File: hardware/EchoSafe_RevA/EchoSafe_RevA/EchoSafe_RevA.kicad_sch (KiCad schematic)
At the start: 37 parts, among them J1 TP4056_Module, M1 C0720B001F, M2 C0720B001F, M3 C0720B001F, M4 C0720B001F, U1 ESP32-S3-WROOM-1-N16R8, U2 MAX98357AETE+T, U3 DRV2605LDGS, U5 TCA9548A, U6 DRV2605LDGS, U7 DRV2605LDGS, U8 DRV2605LDGS

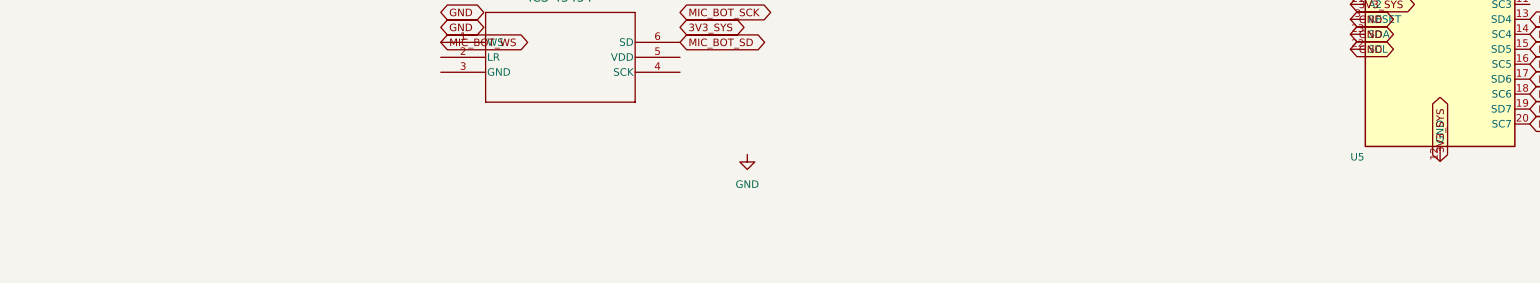
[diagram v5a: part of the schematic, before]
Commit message: Add per-module wire harness connectors (star topology)
Adds J2 (Front-Left, 9 pins), J3 (Front-Right, 9 pins), J4 (Rear-Left,
7 pins), J5 (Rear-Right, 7 pins) -- placeholder generic connectors
documenting the exact conductor count and signal list each earpiece
module's cable needs, per the confirmed board partition:

- Front modules (J2/J3): WS, BCLK, DOUT, 3V3_SYS, GND, motor OUTP/OUTN,
  speaker OUTP/OUTN
- Rear modules (J4/J5): same minus the speaker pair

Star topology confirmed with the user: each module gets its own full
copy of the shared mic I2S bus via a separate cable, rather than one
cable daisy-chaining through both mics on a pair. The electrical nets
are unchanged either way (both mics on a pair always share the same
ESP32 pins) -- the topology choice only affects physical cable routing
and how many pins the central pod's connectors need.

Documented that each mic's SEL pin does not need a dedicated harness
wire (it's a static tie, wired locally using the 3V3_SYS/GND already
present at the module for mic power), and that each mic's decoupling
cap (C9-C12) travels with its mic to the earpiece module rather than
staying centralized -- decoupling only works close to the pin it
protects.

Verified: whole-file paren balance intact, 475 unique UUIDs, no
duplicate references, correct net endpoint counts on every affected
signal, no coordinate conflicts.

Co-Authored-By: Claude Sonnet 5 <noreply@anthropic.com>
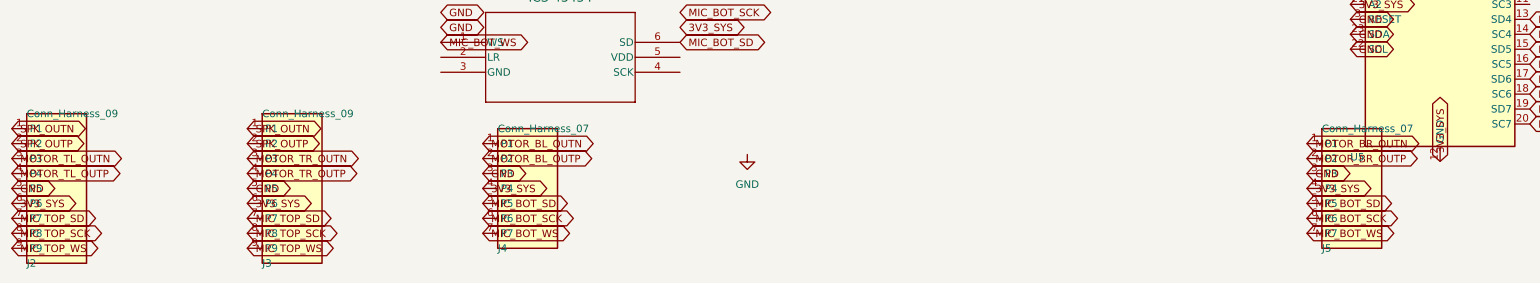
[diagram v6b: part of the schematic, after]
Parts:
- added J2, J3: Conn_Harness_09, symbol Connector:Conn_Harness_09
- added J4, J5: Conn_Harness_07, symbol Connector:Conn_Harness_07
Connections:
- net 3V3_SYS: now also J2.6 (P6), J3.6 (P6), J4.4 (P4), J5.4 (P4)
- net GND: now also J2.5 (P5), J3.5 (P5), J4.3 (P3), J5.3 (P3)
- net MIC_BOT_SCK: now also J4.6 (P6), J5.6 (P6)
- net MIC_BOT_SD: now also J4.5 (P5), J5.5 (P5)
- net MIC_BOT_WS: now also J4.7 (P7), J5.7 (P7)
- net MIC_TOP_SCK: now also J2.8 (P8), J3.8 (P8)
- net MIC_TOP_SD: now also J2.7 (P7), J3.7 (P7)
- net MIC_TOP_WS: now also J2.9 (P9), J3.9 (P9)
- net MOTOR_BL_OUTN: now also J4.1 (P1)
- net MOTOR_BL_OUTP: now also J4.2 (P2)
- net MOTOR_BR_OUTN: now also J5.1 (P1)
- net MOTOR_BR_OUTP: now also J5.2 (P2)
- net MOTOR_TL_OUTN: now also J2.3 (P3)
- net MOTOR_TL_OUTP: now also J2.4 (P4)
- net MOTOR_TR_OUTN: now also J3.3 (P3)
- net MOTOR_TR_OUTP: now also J3.4 (P4)
- net SPK_OUTN: now also J2.1 (P1), J3.1 (P1)
- net SPK_OUTP: now also J2.2 (P2), J3.2 (P2)

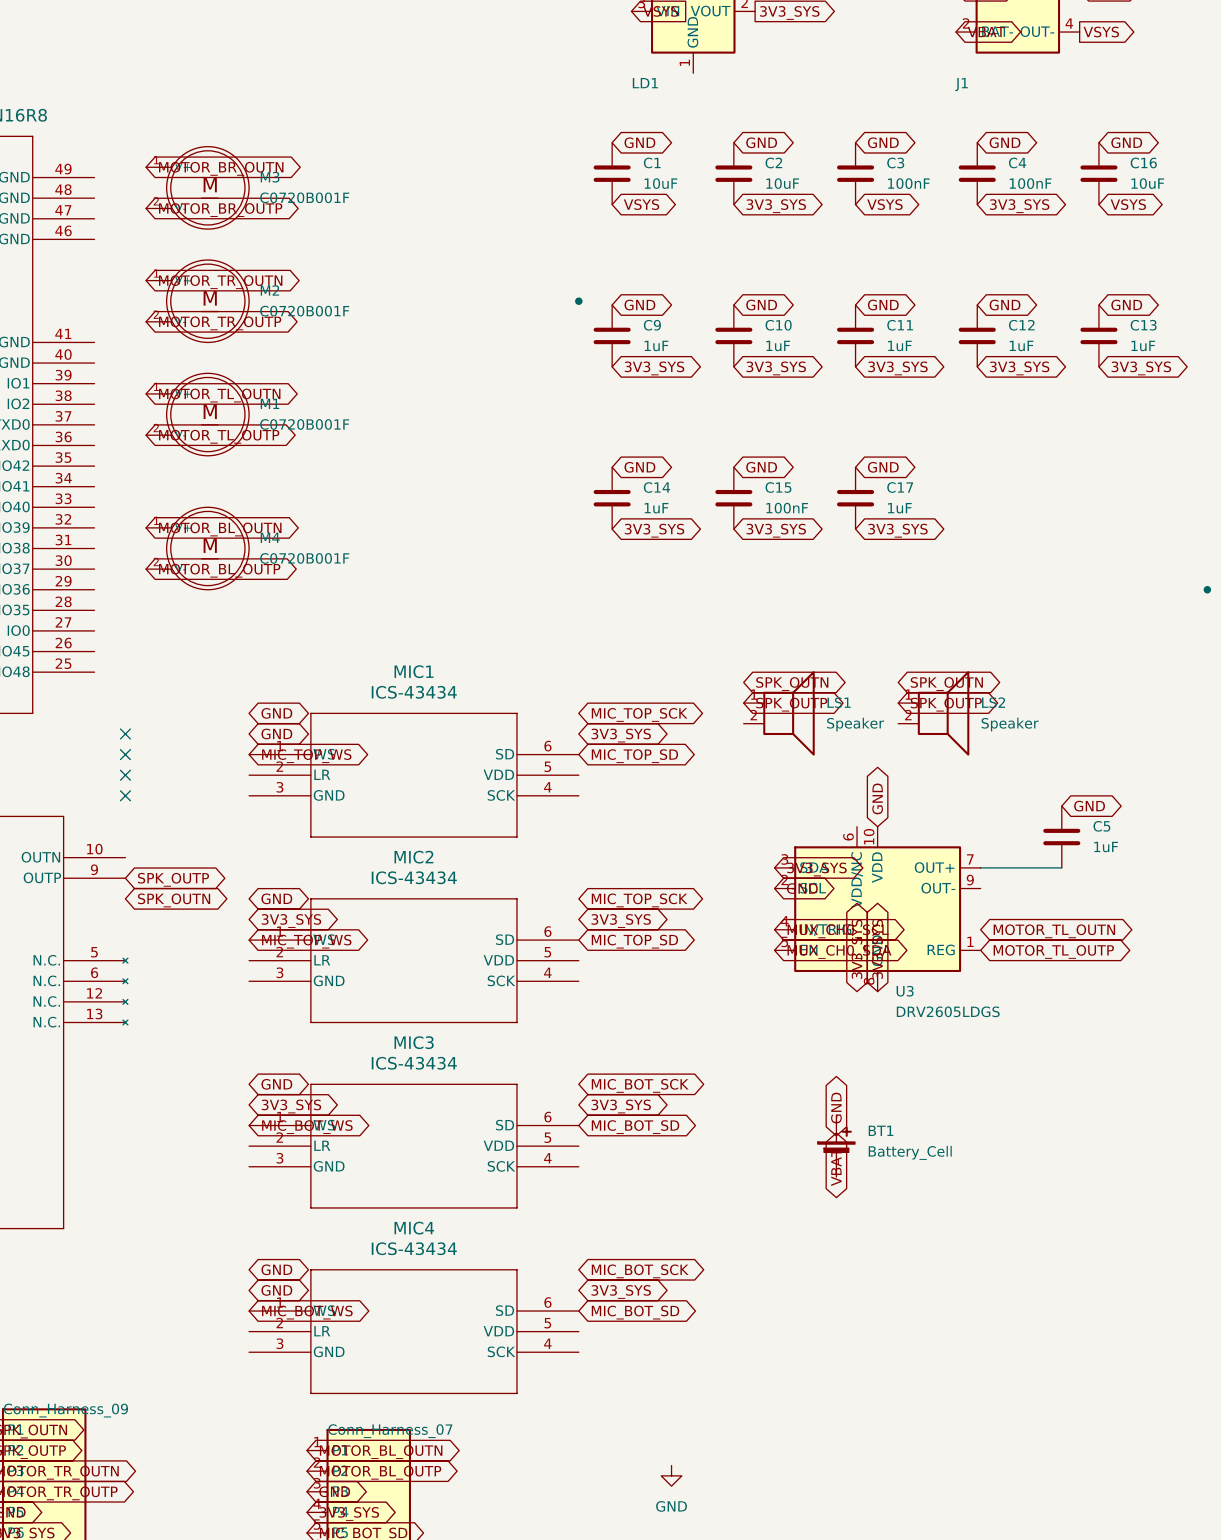
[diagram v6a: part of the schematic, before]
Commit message: Split hardware into 5 separate KiCad projects (central pod + 4 modules)
EchoSafe_RevA now specifically represents the central pod. Created 4 new
small KiCad projects for the earpiece modules, each with its own
.kicad_pro/.kicad_sch/sym-lib-table:

- EchoSafe_FrontLeft:  MIC1, M1, LS1, C9  (9-pin connector, has speaker)
- EchoSafe_FrontRight: MIC2, M2, LS2, C10 (9-pin connector, has speaker)
- EchoSafe_RearLeft:   MIC4, M4, C12      (7-pin connector, no speaker)
- EchoSafe_RearRight:  MIC3, M3, C11      (7-pin connector, no speaker)

All 4 new projects share the existing library folder
(EchoSafe_RevA/lib/symbols/) via relative sym-lib-table paths -- nothing
duplicated. Each module has its own local J1 connector wired with the
same net names as the corresponding pod-side connector (J2/J3/J4/J5);
matching names is a documentation convention across independent
projects, not an automatic KiCad link -- the physical cable is the real
connection.

Removed MIC1-4, M1-4, LS1-2, and C9-C12 (their decoupling caps) from the
central pod's schematic entirely -- both the component instances and
their pin-level net labels -- verifying net-by-net that only the
endpoints which moved out were removed (e.g. MIC_TOP_WS dropped from 5
endpoints to 3: ESP32 + the two pod-side connectors, matching what
should remain).

Verified independently: all 5 .kicad_sch files have balanced parens and
unique UUIDs within their own file (no cross-project uniqueness
requirement -- separate projects, separate namespaces); the central
pod's shared nets (3V3_SYS, GND, motor/speaker/mic buses) retain exactly
the endpoints that should still be there.

Co-Authored-By: Claude Sonnet 5 <noreply@anthropic.com>
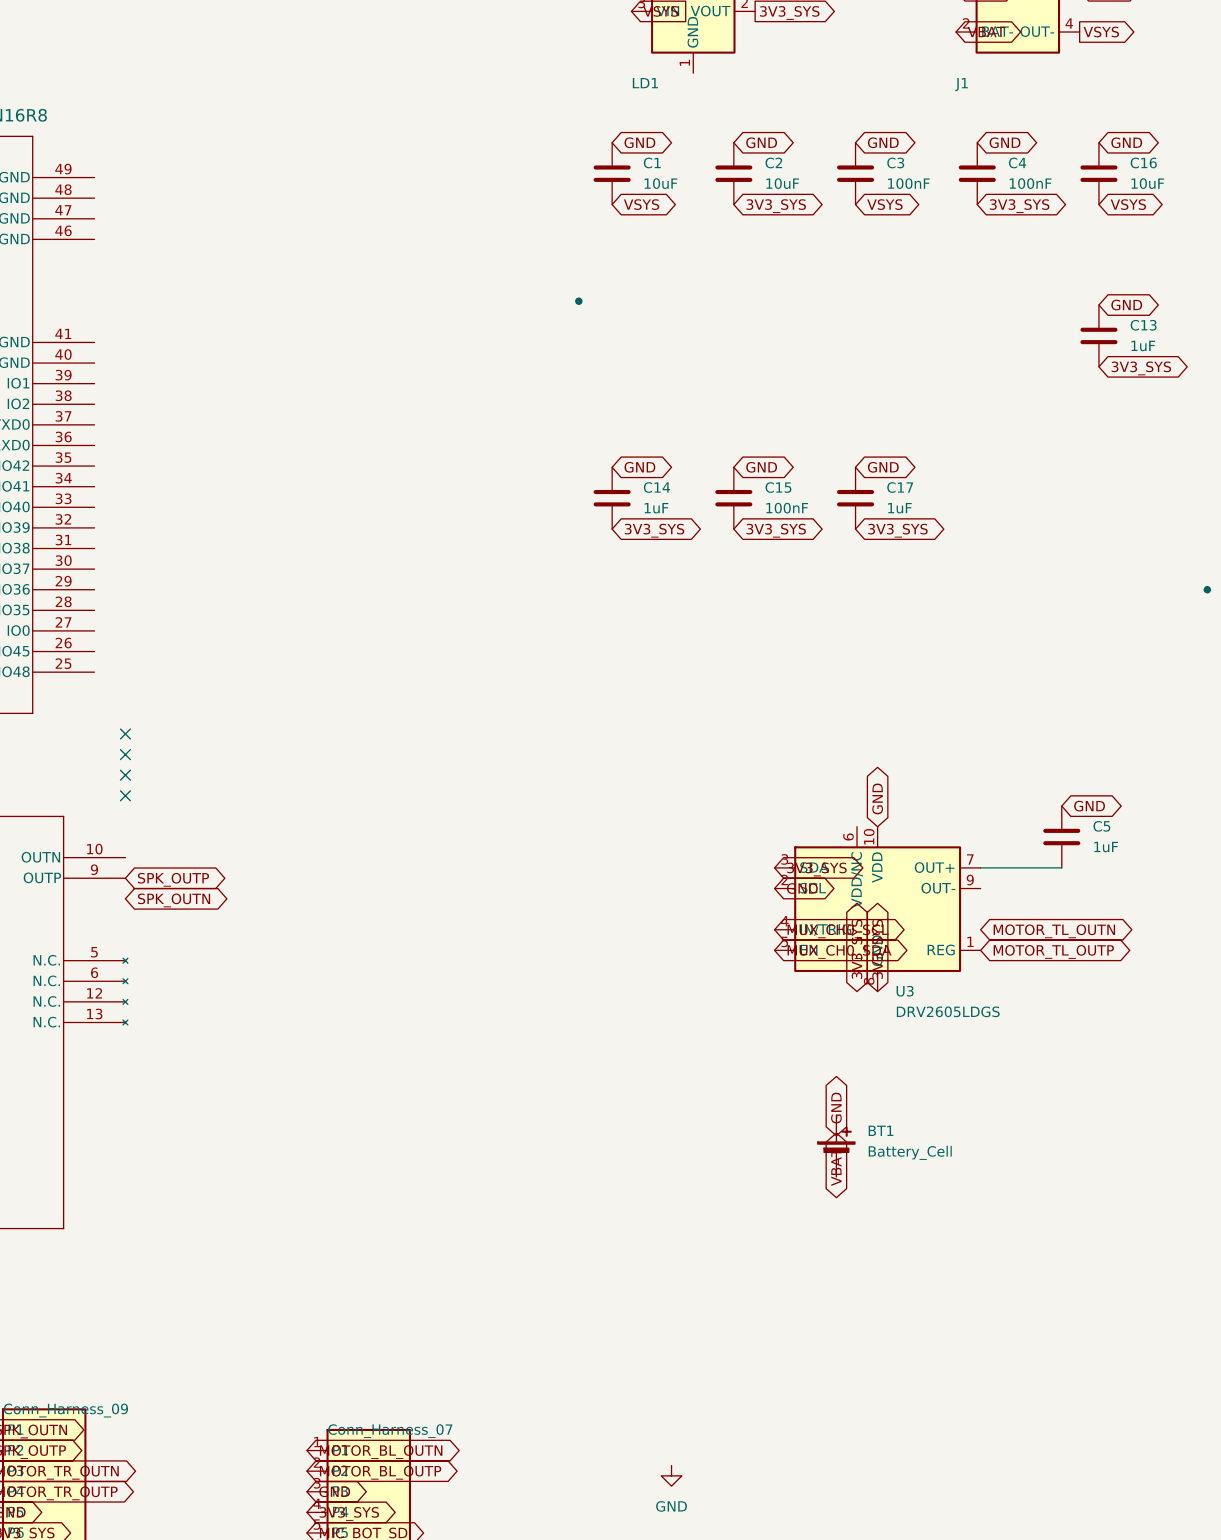
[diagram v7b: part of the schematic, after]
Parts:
- removed C10, C11, C12, C9: 1uF, symbol Device:C
- removed LS1, LS2: Speaker, symbol Device:Speaker
- removed M1, M2, M3, M4: C0720B001F, C0720B001F:XDCR_C0720B001F, symbol haptic_motors:C0720B001F
- removed MIC1, MIC2, MIC3, MIC4: ICS-43434, LGA_CAV_IVS, symbol Mics:ICS-43434

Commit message: Assign footprints across all 5 projects, add missing fp-lib-table
Target confirmed as a compact near-final wearable, not an early bring-up
prototype -- choices below favor small/soldered over socketed/header.

Fixed a regression: splitting into 5 projects had wiped the mic
(LGA_CAV_IVS) and motor (C0720B001F:XDCR_C0720B001F) footprints that
already existed pre-split -- the instance generator zeroed every new
component's footprint unconditionally. Restored both from the pre-split
commit.

Fixed a second, pre-existing bug: no fp-lib-table ever existed in any
version of this project (same class of gap as the sym-lib-table issue
found earlier this session), and three footprint references
(LGA_CAV_IVS, ESP32-S3-WROOM-1_EXP, 21-0136I_T1633-4_MXM) were bare
names with no library prefix -- neither would have resolved in KiCad's
PCB editor even with a table present. Created fp-lib-table in the
central pod (ESP32-S3-WROOM-1, MAX98357AETE-T) and all 4 module projects
(ICS-43434, C0720B001F), then added the missing prefixes. Verified every
path resolves to a real .kicad_mod file on disk.

Newly assigned:
- All 17 capacitors -> Capacitor_SMD:C_0603_1608Metric
- BT1 (battery) -> Connector_JST:JST_PH_S2B_PH_K_1x02_P2.00mm_Horizontal
  (confirmed: this battery ships with a pre-attached JST-PH connector)
- LD1 (LD1117V33) -> 3-pin 2.54mm header pattern (matches the real
  breakout's hole spacing regardless of pins-vs-wire assembly)
- J1/central pod (TP4056) -> 4-pin 2.54mm header pattern (placeholder --
  flagged to verify against the actual purchased board's hole spacing)
- J2-J5 (pod) + each module's J1 -> JST-SH 1.0mm pitch, 9-pin or 7-pin
  (compact-wearable target ruled out bulkier 2.54mm headers for a
  7-9-conductor cable through the headband)

Left unassigned: LS1/LS2 (speakers) -- no specific part chosen yet,
capsule dimensions vary too much to guess a meaningful footprint.

Verified across all 5 files independently: paren balance intact, no
duplicate UUIDs, no duplicate re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
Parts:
- BT1: footprint (none) -> Connector_JST:JST_PH_S2B_PH_K_1x02_P2.00mm_Horizontal
- C1, C13, C14, C15, C16, C17, C2, C3, C4, C5, C6, C7, C8: footprint (none) -> Capacitor_SMD:C_0603_1608Metric
- J1: footprint (none) -> Connector_PinHeader_2.54mm:PinHeader_1x04_P2.54mm_Vertical
- J2, J3: footprint (none) -> Connector_JST:JST_SH_BM09B-SRSS-TB_1x09-1MP_P1.00mm_Horizontal
- J4, J5: footprint (none) -> Connector_JST:JST_SH_BM07B-SRSS-TB_1x07-1MP_P1.00mm_Horizontal
- LD1: footprint (none) -> Connector_PinHeader_2.54mm:PinHeader_1x03_P2.54mm_Vertical
- U1: footprint ESP32-S3-WROOM-1_EXP -> ESP32-S3-WROOM-1:ESP32-S3-WROOM-1_EXP
- U2: footprint 21-0136I_T1633-4_MXM -> MAX98357AETE-T:21-0136I_T1633-4_MXM
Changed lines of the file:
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@@
 			)
 		)
-		(property "Footprint" ""
+		(property "Footprint" "Connector_JST:JST_PH_S2B_PH_K_1x02_P2.00mm_Horizontal"
 			(at 167.64 149.606 90)
 			(effects
@@
 			)
 		)
-		(property "Footprint" "ESP32-S3-WROOM-1_EXP"
+		(property "Footprint" "ESP32-S3-WROOM-1:ESP32-S3-WROOM-1_EXP"
 			(at 35.56 30.48 0)
 			(effects
@@
 			)
 		)
-		(property "Footprint" "21-0136I_T1633-4_MXM"
+		(property "Footprint" "MAX98357AETE-T:21-0136I_T1633-4_MXM"
 			(at 29.21 116.84 0)
 			(effects
@@
 	(no_connect (at 80.01 104.14))
 	(no_connect (at 80.01 101.6))
-	(no_connect (at 80.01 99.06))	(symbol
+	(no_connect (at 80.01 99.06))
+	(symbol
 		(lib_id "Device:C")
 		(at 195.42 111.76 0)
@@
 			)
 		)
-		(property "Footprint" ""
+		(property "Footprint" "Capacitor_SMD:C_0603_1608Metric"
 			(at 195.42 111.76 0)
 			(effects
@@
 			)
 		)
-		(property "Footprint" ""
+		(property "Footprint" "Capacitor_SMD:C_0603_1608Metric"
 			(at 277.7 31.11 0)
 			(effects
@@
 			)
 		)
-		(property "Footprint" ""
+		(property "Footprint" "Capacitor_SMD:C_0603_1608Metric"
 			(at 277.7 66.11 0)
 			(effects
@@
 			)
 		)
-		(property "Footprint" ""
+		(property "Footprint" "Capacitor_SMD:C_0603_1608Metric"
 			(at 277.7 101.11 0)
 			(effects
@@
 			(effects (font (size 1.27 1.27)) (justify left))
 		)
-		(property "Footprint" ""
+		(property "Footprint" "Connector_PinHeader_2.54mm:PinHeader_1x03_P2.54mm_Vertical"
 			(at 150 10 0)
 			(effects (font (size 1.27 1.27) (italic yes)) (hide yes))
@@
 			(effects (font (size 1.27 1.27)) (justify left))
 		)
-		(property "Footprint" ""
+		(property "Footprint" "Connector_PinHeader_2.54mm:PinHeader_1x04_P2.54mm_Vertical"
 			(at 190 10 0)
 			(effects (font (size 1.27 1.27) (italic yes)) (hide yes))
@@
 			)
 		)
-		(property "Footprint" ""
+		(property "Footprint" "Capacitor_SMD:C_0603_1608Metric"
 			(at 140 30 0)
 			(effects
@@
 			)
 		)
-		(property "Footprint" ""
+		(property "Footprint" "Capacitor_SMD:C_0603_1608Metric"
 			(at 155 30 0)
 			(effects
@@
 			)
 		)
-		(property "Footprint" ""
+		(property "Footprint" "Capacitor_SMD:C_0603_1608Metric"
 			(at 170 30 0)
 			(effects
@@
 			)
 		)
-		(property "Footprint" ""
+		(property "Footprint" "Capacitor_SMD:C_0603_1608Metric"
 			(at 185 30 0)
 			(effects
@@
 			)
 		)
-		(property "Footprint" ""
+		(property "Footprint" "Capacitor_SMD:C_0603_1608Metric"
 			(at 200 30 0)
 			(effects
@@
 			)
 		)
-		(property "Footprint" ""
+		(property "Footprint" "Capacitor_SMD:C_0603_1608Metric"
 			(at 200 50 0)
 			(effects
@@
 			)
 		)
-		(property "Footprint" ""
+		(property "Footprint" "Capacitor_SMD:C_0603_1608Metric"
 			(at 140 70 0)
 			(effects
@@
 			)
 		)
-		(property "Footprint" ""
+		(property "Footprint" "Capacitor_SMD:C_0603_1608Metric"
 			(at 155 70 0)
 			(effects
@@
 			)
 		)
-		(property "Footprint" ""
+		(property "Footprint" "Capacitor_SMD:C_0603_1608Metric"
 			(at 170 70 0)
 			(effects
@@
 			(effects (font (size 1.27 1.27)) (justify left))
 		)
-		(property "Footprint" ""
+		(property "Footprint" "Connector_JST:JST_SH_BM09B-SRSS-TB_1x09-1MP_P1.00mm_Horizontal"
 			(at 30 195 0)
 			(effects (font (size 1.27 1.27) (italic yes)) (hide yes))
@@
 			(effects (font (size 1.27 1.27)) (justify left))
 		)
-		(property "Footprint" ""
+		(property "Footprint" "Connector_JST:JST_SH_BM09B-SRSS-TB_1x09-1MP_P1.00mm_Horizontal"
 			(at 70 195 0)
 			(effects (font (size 1.27 1.27) (italic yes)) (hide yes))
@@
 			(effects (font (size 1.27 1.27)) (justify left))
 		)
-		(property "Footprint" ""
+		(property "Footprint" "Connector_JST:JST_SH_BM07B-SRSS-TB_1x07-1MP_P1.00mm_Horizontal"
 			(at 110 195 0)
 			(effects (font (size 1.27 1.27) (italic yes)) (hide yes))
@@
 			(effects (font (size 1.27 1.27)) (justify left))
 		)
-		(property "Footprint" ""
+		(property "Footprint" "Connector_JST:JST_SH_BM07B-SRSS-TB_1x07-1MP_P1.00mm_Horizontal"
 			(at 250 195 0)
 			(effects (font (size 1.27 1.27) (italic yes)) (hide yes))
